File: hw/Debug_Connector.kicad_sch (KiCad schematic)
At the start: 1 part, among them J5 Debug

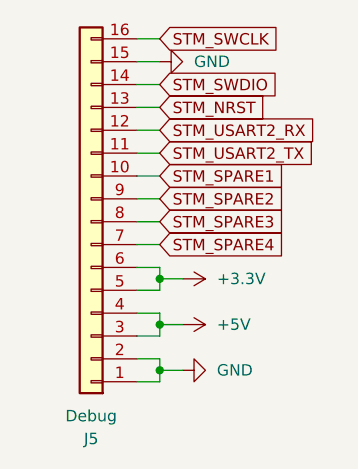
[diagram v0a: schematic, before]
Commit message: added new LED traces to hardware
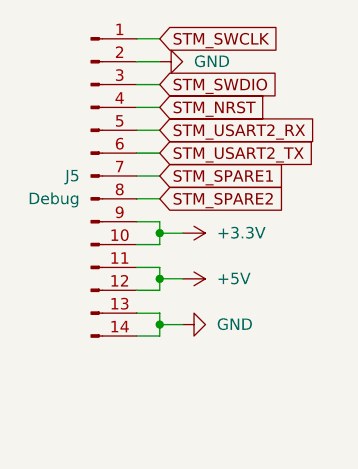
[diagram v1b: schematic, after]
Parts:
- removed J5: Debug, Connector_PinHeader_2.54mm:PinHeader_1x16_P2.54mm_Vertical, symbol Connector_Generic:Conn_01x16
- added J5: Debug, Connector_PinHeader_2.54mm:PinHeader_1x14_P2.54mm_Vertical, symbol Connector:Conn_01x14_Pin
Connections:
- net +3.3V: now also J5.10 (Pin_10), J5.9 (Pin_9)
- net +5V: now also J5.11 (Pin_11), J5.12 (Pin_12)
- net GND: now also J5.13 (Pin_13), J5.14 (Pin_14), J5.2 (Pin_2)
- net STM_NRST: now also J5.4 (Pin_4)
- net STM_SPARE1: now also J5.7 (Pin_7)
- net STM_SPARE2: now also J5.8 (Pin_8)
- net STM_SWCLK: now also J5.1 (Pin_1)
- net STM_SWDIO: now also J5.3 (Pin_3)
- net STM_USART2_RX: now also J5.5 (Pin_5)
- net STM_USART2_TX: now also J5.6 (Pin_6)
